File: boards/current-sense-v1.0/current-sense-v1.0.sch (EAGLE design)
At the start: 90 parts, among them IC1 ISO7241, IC2 ISO7241, IC3 ISO7242, IC4 ISO7240, J1 4-PIN_2MM-H, J2 MKS-1658, J3 8-PIN_2MM-H, J6 DF22-2, Q1 IRFH7545, Q2 IRFH7545, Q3 IRFH7545, Q4 IRFH7545, Q5 IRFH7545, Q6 IRFH7545, U1 DRV8303DCA, U13 TLV70233DBVR, U2 INA240PWR, U3 INA240PWR, U4 INA240PWR, U5 TLV70233DBVR, U6 ADS8028IRTJT, U7 MPM3620GQV-P, U8 VND5E006ASPTR-E, U9 TLV70450

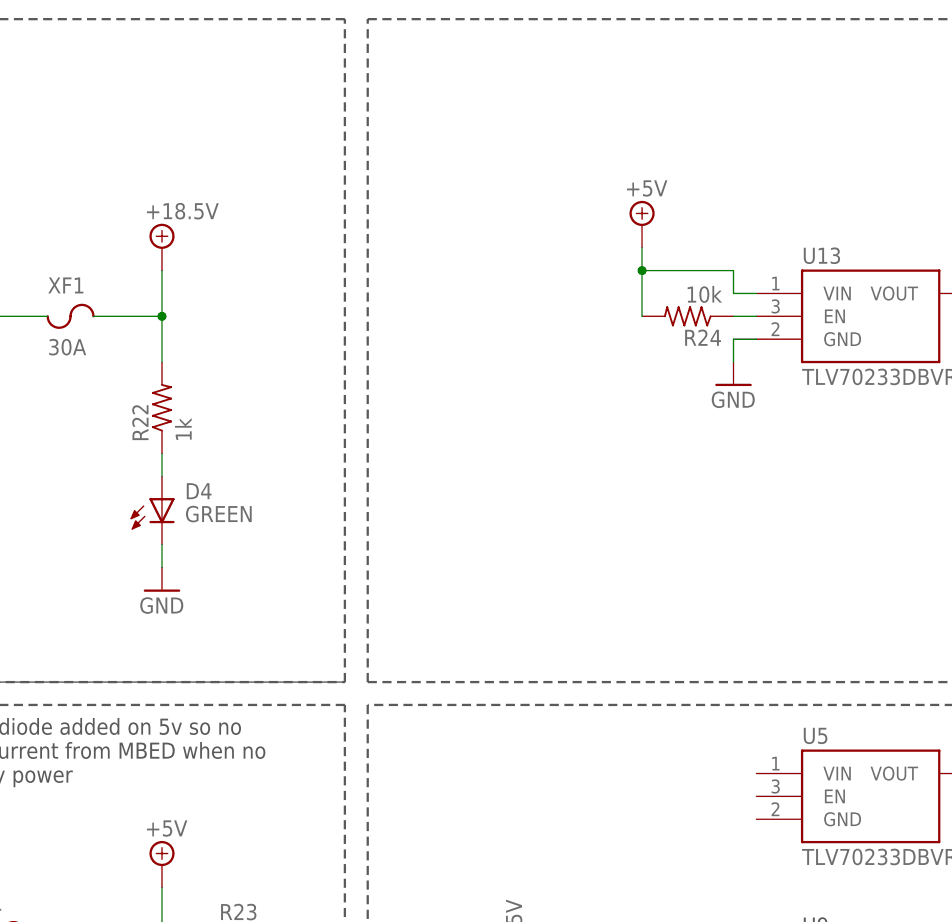
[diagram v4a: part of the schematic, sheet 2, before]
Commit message: added names to some borders
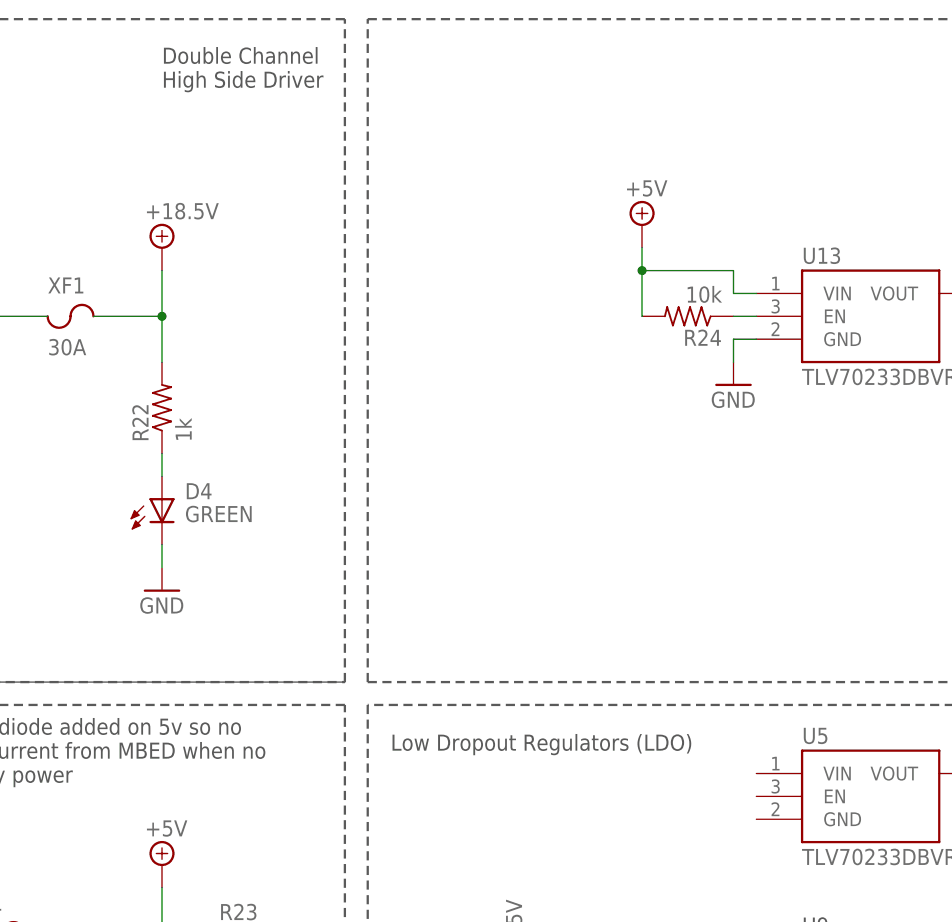
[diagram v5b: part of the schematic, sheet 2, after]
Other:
- note added: "Digital Isolators"
- note added: "Double Channel High Side Driver"
- note added: "Internal Temperature Sensor"
- note added: "Low Dropout Regulators (LDO)"
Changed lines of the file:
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@@
 <wire x1="165.1" y1="124.46" x2="165.1" y2="73.66" width="0.254" layer="97" style="shortdash"/>
 <wire x1="165.1" y1="73.66" x2="165.1" y2="63.5" width="0.254" layer="97" style="shortdash"/>
+<text x="167.64" y="119.38" size="1.778" layer="97">Low Dropout Regulators (LDO)</text>
+<text x="142.24" y="193.04" size="1.778" layer="97">Double Channel
+High Side Driver</text>
 </plain>
 <instances>
@@
 <wire x1="266.7" y1="43.18" x2="127" y2="43.18" width="0.254" layer="97" style="shortdash"/>
 <wire x1="127" y1="43.18" x2="127" y2="63.5" width="0.254" layer="97" style="shortdash"/>
+<text x="20.32" y="193.04" size="1.778" layer="97">Digital Isolators</text>
+<text x="129.54" y="193.04" size="1.778" layer="97">Internal Temperature Sensor</text>
 </plain>
 <instances>
